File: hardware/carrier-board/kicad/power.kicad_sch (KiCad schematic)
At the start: 0 parts

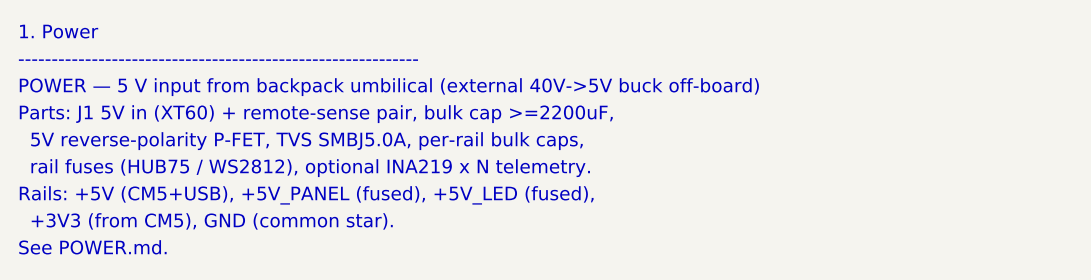
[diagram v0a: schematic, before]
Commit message: Carrier docs + KiCad plan: full two-brain pass (CM5 HUB75 + RP2354B I/O)
Propagate the two-brain architecture across the whole doc set and KiCad plan:
- REQUIREMENTS: restructured M1-M12 (CM5 HUB75; RP2354B core/MAX7219/WS2812/
  sensors/buttons/servos; USB selector + standalone program port); N-list reworked.
- POWER: add +V_SERVO and +3V3_RP rails, servo current budget, updated worked
  total + protection; sensors now on +3V3_RP not CM5 3V3.
- CONNECTORS: J3 re-sourced to RP2354B SPI0, J4 4 WS2812 zones, J5 +SENS_INT,
  J6 BTN1..10, add J12 USB-C, J20-J27 servos, SW1 USB selector, SWD/UART hdrs;
  drop JP1/JP2; fans presented as RP2354B-default-or-CM5 (decision flagged).
- BOM: add RP2354B core, '125/'245 (RP side), USB mux/USB-C/ESD, servo headers,
  +3V3_RP reg; fix '125 double-count and stale HUB75/MAX7219-shared-buffer/JP1.
- MULTI-BACKEND: HUB75+MAX7219 now simultaneous (different brains); firmware
  CompositePanelOutput is the sole remaining blocker.
- IO-EXPANSION: RP2354B is the primary I/O backbone; I2C expanders secondary.
- kicad: 11-sheet plan, stable UUIDs, generator skips populated face_buffer.
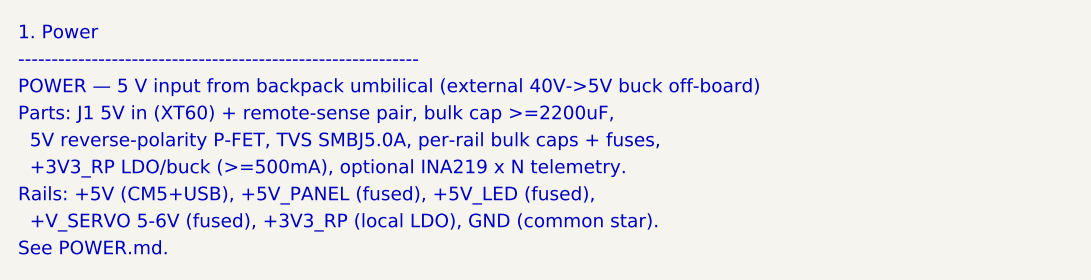
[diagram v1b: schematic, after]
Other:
- note added: "+3V3_RP LDO/buck (>=500mA), optional INA219 x N telemetry."
- note added: "+V_SERVO 5-6V (fused), +3V3_RP (local LDO), GND (common star)."
- note added: "5V reverse-polarity P-FET, TVS SMBJ5.0A, per-rail bulk caps + fuses,"
- note removed: "+3V3 (from CM5), GND (common star)."
- note removed: "5V reverse-polarity P-FET, TVS SMBJ5.0A, per-rail bulk caps,"
- note removed: "rail fuses (HUB75 / WS2812), optional INA219 x N telemetry."
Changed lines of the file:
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@@
   (text "POWER — 5 V input from backpack umbilical (external 40V->5V buck off-board)" (at 25.4 31.40 0) (effects (font (size 1.5 1.5)) (justify left bottom)))
   (text "Parts: J1 5V in (XT60) + remote-sense pair, bulk cap >=2200uF," (at 25.4 34.40 0) (effects (font (size 1.5 1.5)) (justify left bottom)))
-  (text "  5V reverse-polarity P-FET, TVS SMBJ5.0A, per-rail bulk caps," (at 25.4 37.40 0) (effects (font (size 1.5 1.5)) (justify left bottom)))
-  (text "  rail fuses (HUB75 / WS2812), optional INA219 x N telemetry." (at 25.4 40.40 0) (effects (font (size 1.5 1.5)) (justify left bottom)))
+  (text "  5V reverse-polarity P-FET, TVS SMBJ5.0A, per-rail bulk caps + fuses," (at 25.4 37.40 0) (effects (font (size 1.5 1.5)) (justify left bottom)))
+  (text "  +3V3_RP LDO/buck (>=500mA), optional INA219 x N telemetry." (at 25.4 40.40 0) (effects (font (size 1.5 1.5)) (justify left bottom)))
   (text "Rails: +5V (CM5+USB), +5V_PANEL (fused), +5V_LED (fused)," (at 25.4 43.40 0) (effects (font (size 1.5 1.5)) (justify left bottom)))
-  (text "  +3V3 (from CM5), GND (common star)." (at 25.4 46.40 0) (effects (font (size 1.5 1.5)) (justify left bottom)))
+  (text "  +V_SERVO 5-6V (fused), +3V3_RP (local LDO), GND (common star)." (at 25.4 46.40 0) (effects (font (size 1.5 1.5)) (justify left bottom)))
   (text "See POWER.md." (at 25.4 49.40 0) (effects (font (size 1.5 1.5)) (justify left bottom)))
   (sheet_instances

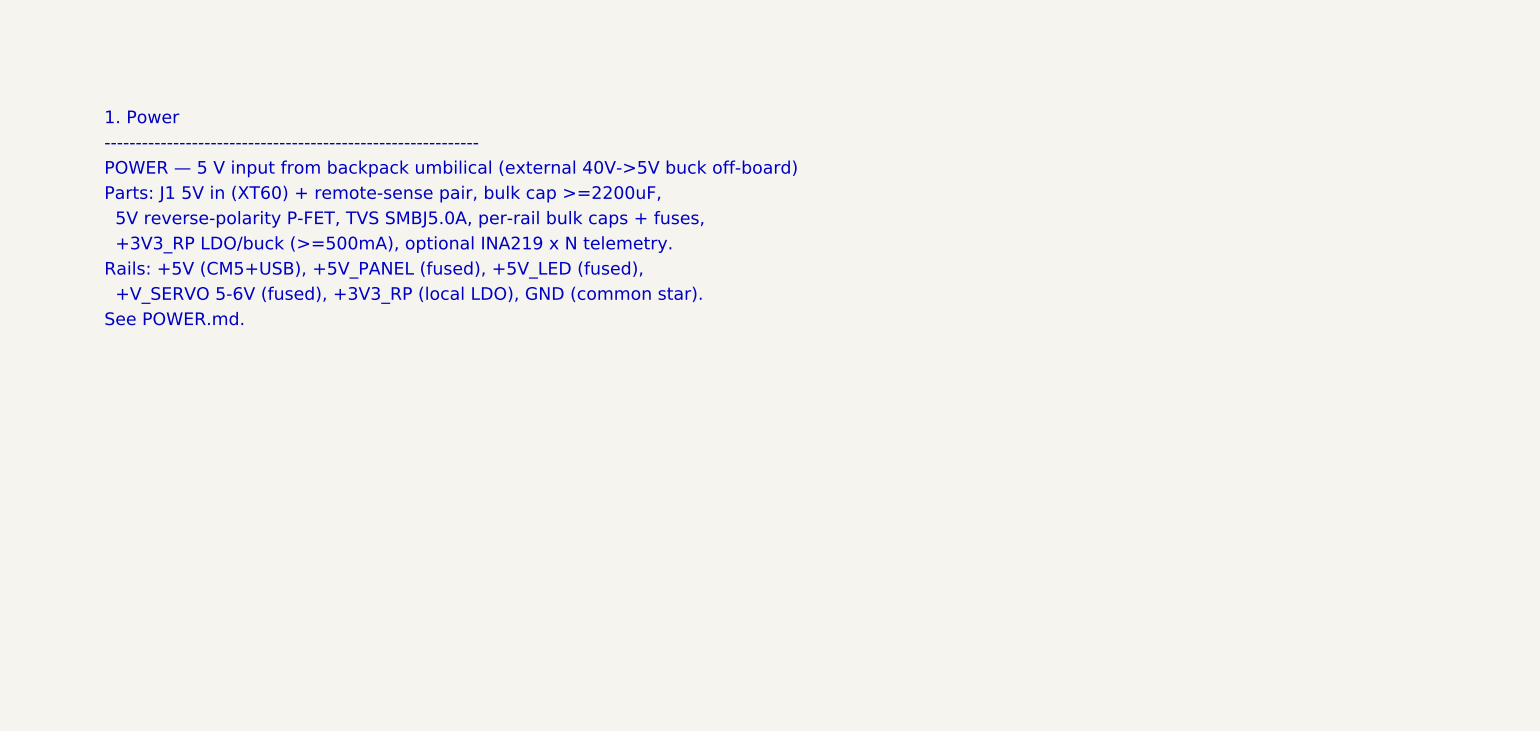
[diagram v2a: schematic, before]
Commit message: Carrier KiCad: populate all 11 schematic sheets
Replace populate_face_buffer.py with populate_sheets.py: one generator that
emits all 11 populated sub-sheets reusing the KiCad-9 format proven by the
face_buffer proof. Shared symbol library + generic box-symbol builder; condensed
CM5 (2x DF40-100) and RP2354B (QFN-80) symbols showing only used pins.

Connectivity by net labels (global for rails + cross-sheet nets: GPIOxx HUB75,
MX_*, LED*_DAT, SRV*, BTN*, *_USB_*; local within-sheet). Sheets: power
(protection + rails + AP2112 +3V3_RP), cm5 (HUB75 out + fan MOSFETs + RP ctrl),
face_buffer, rp2354_io (RP2354B + xtal + SW1/J12 + ESD + SWD), rp2354_face
(U10->J3), leds (U11 quad ->J4a-d), sensors_i2c (pull-ups+J5+STEMMA),
servos (J20-27 + rail), gpio_buttons (J6), usb (USB2514B hub + uplink),
cameras_display (CSI FFC + HDMI).

Verified: all sheets paren-balanced, every used lib_id defined, all instance
paths match sheet UUIDs, root<->sub-sheet UUID linkage intact. generate_skeleton.py
now lists all sheets POPULATED (writes only root+project). Not yet opened in
KiCad here -- expect ERC warnings (PWR_FLAG, unconnected pins) to clean.
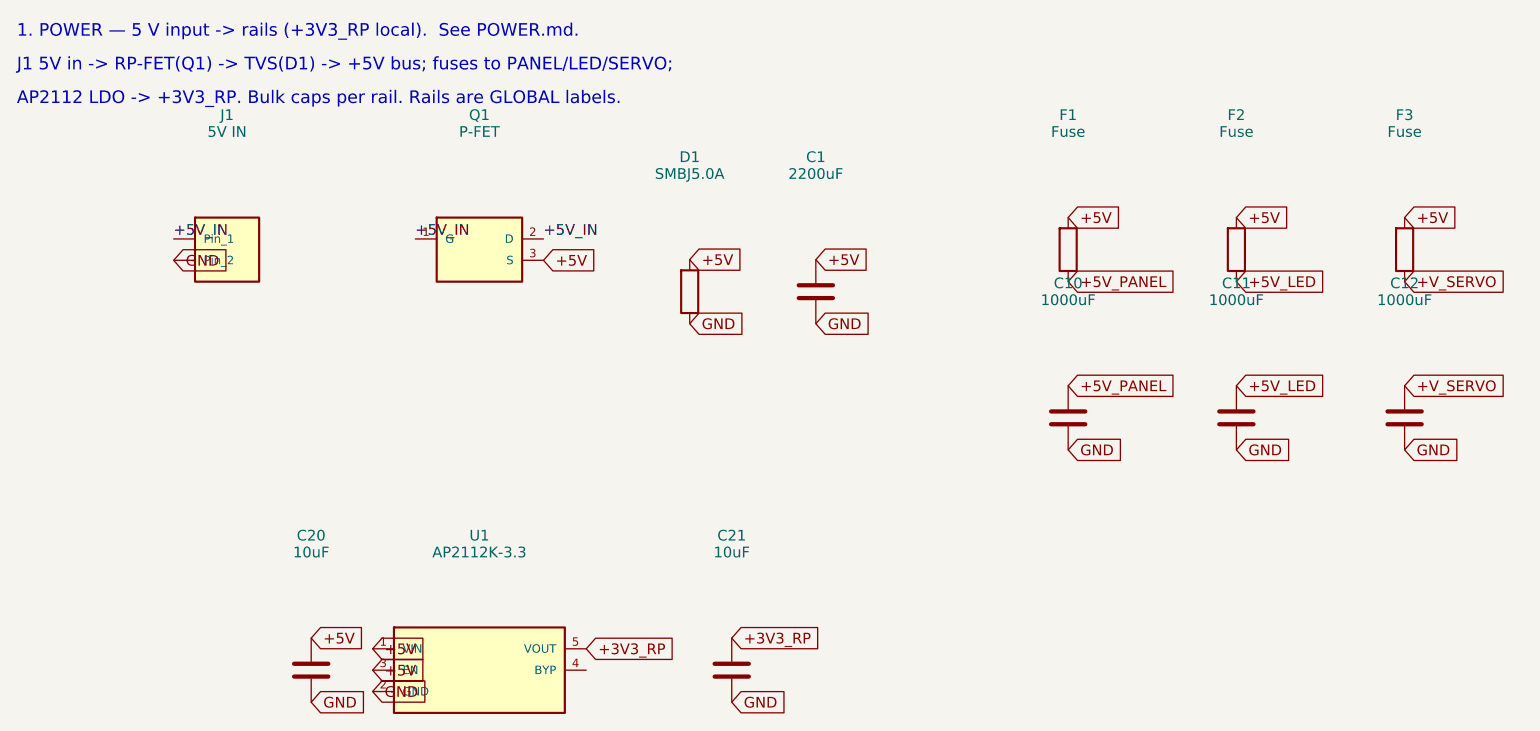
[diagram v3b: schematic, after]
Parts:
- added C1: 2200uF, symbol Device:C
- added C10, C11, C12: 1000uF, symbol Device:C
- added C20, C21: 10uF, symbol Device:C
- added D1: SMBJ5.0A, symbol Device:D_TVS
- added F1, F2, F3: Fuse, symbol Device:Fuse
- added J1: 5V IN, symbol Connector_Generic:Conn_01x02
- added Q1: P-FET, symbol Device:Q_PMOS_GSD
- added U1: AP2112K-3.3, symbol Regulator_Linear:AP2112K-3.3
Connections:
- new net +3V3_RP: C21.1, U1.5 (VOUT)
- new net +5V: C1.1, C20.1, D1.1, F1.1, F2.1, F3.1, Q1.3 (S), U1.1 (VIN), U1.3 (EN)
- new net +5V_IN: J1.1 (Pin_1), Q1.1 (G), Q1.2 (D)
- new net +5V_LED: C11.1, F2.2
- new net +5V_PANEL: C10.1, F1.2
- new net +V_SERVO: C12.1, F3.2
- new net GND: C1.2, C10.2, C11.2, C12.2, C20.2, C21.2, D1.2, J1.2 (Pin_2), U1.2 (GND)
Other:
- note added: "1. POWER — 5 V input -> rails (+3V3_RP local). See POWER.md."
- note added: "AP2112 LDO -> +3V3_RP. Bulk caps per rail. Rails are GLOBAL labels."
- note added: "J1 5V in -> RP-FET(Q1) -> TVS(D1) -> +5V bus; fuses to PANEL/LED/SERVO;"
- note removed: "+3V3_RP LDO/buck (>=500mA), optional INA219 x N telemetry."
- note removed: "+V_SERVO 5-6V (fused), +3V3_RP (local LDO), GND (common star)."
- note removed: "------------------------------------------------------------"
- note removed: "1. Power"
- note removed: "5V reverse-polarity P-FET, TVS SMBJ5.0A, per-rail bulk caps + fuses,"
- note removed: "POWER — 5 V input from backpack umbilical (external 40V->5V buck off-board)"
- note removed: "Parts: J1 5V in (XT60) + remote-sense pair, bulk cap >=2200uF,"
- note removed: "Rails: +5V (CM5+USB), +5V_PANEL (fused), +5V_LED (fused),"
- note removed: "See POWER.md."
